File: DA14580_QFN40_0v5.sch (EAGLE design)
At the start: 29 parts, among them CON1 CON_TC2030-CTL-NL, IC1 1265-1137-1-ND, IC2 NC7SZ00M5XCT-ND, IC3 IC_LDO_XX1117_5, Q1 728-1076-1-ND, Q2 887-1833-1-ND, U1 DA14583-AT2, X1 SSW-114-02-S-S, X2 SSW-114-02-S-S

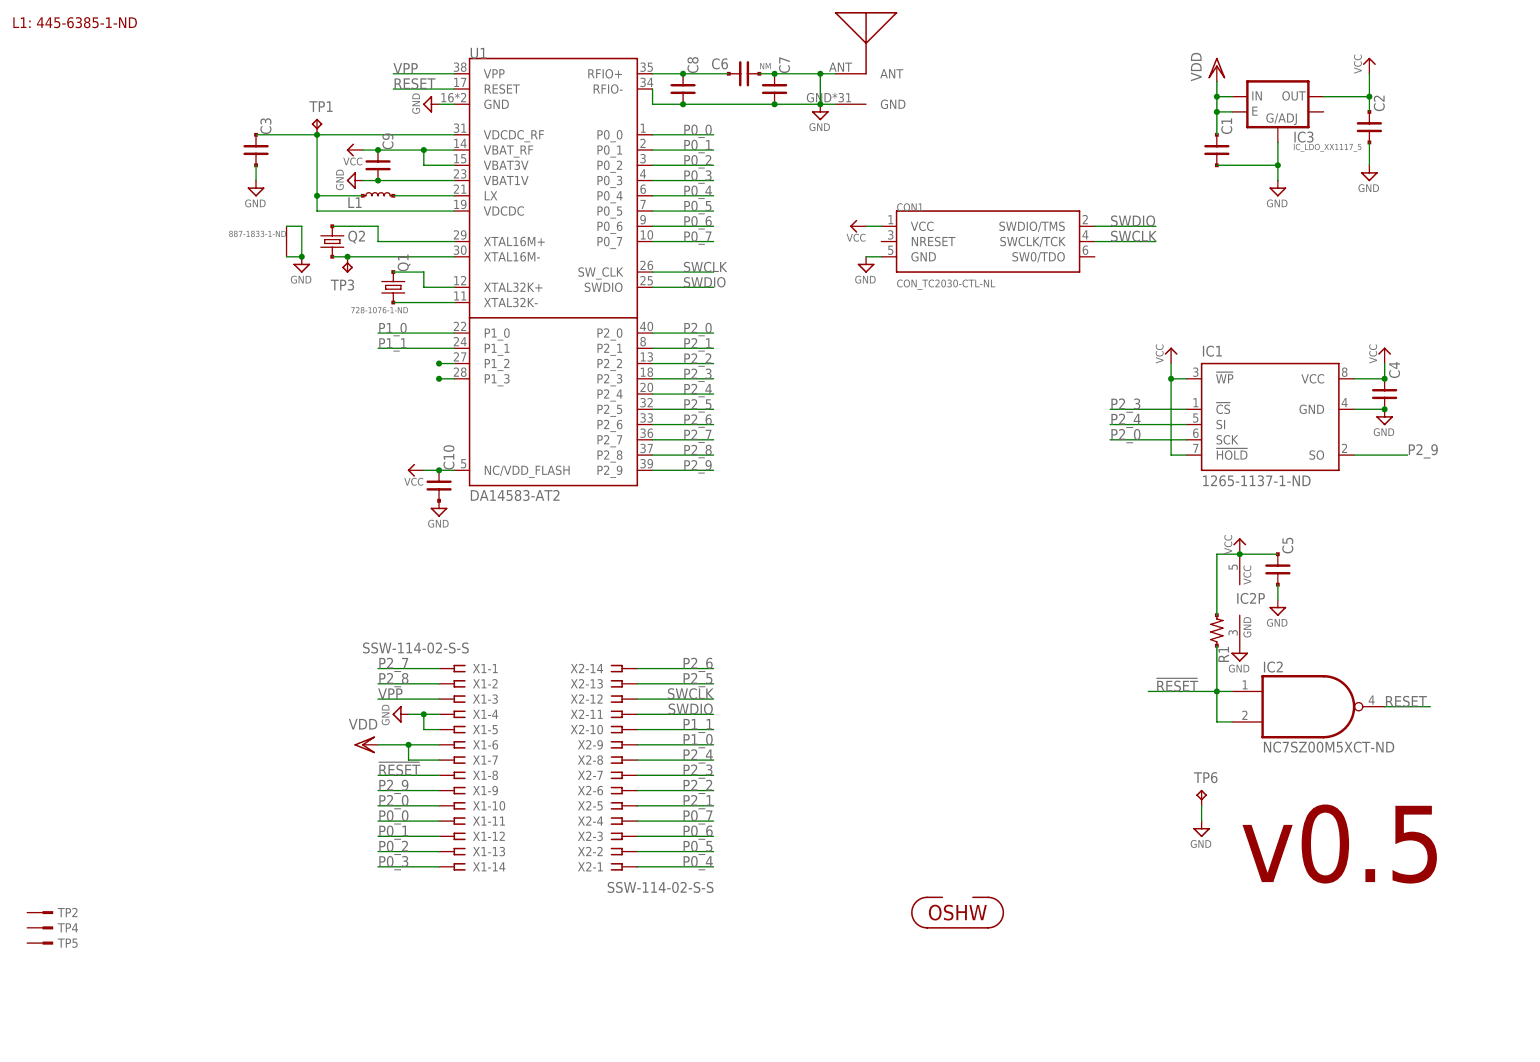
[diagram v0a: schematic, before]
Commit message: update eagle version: 7.5.0; library update
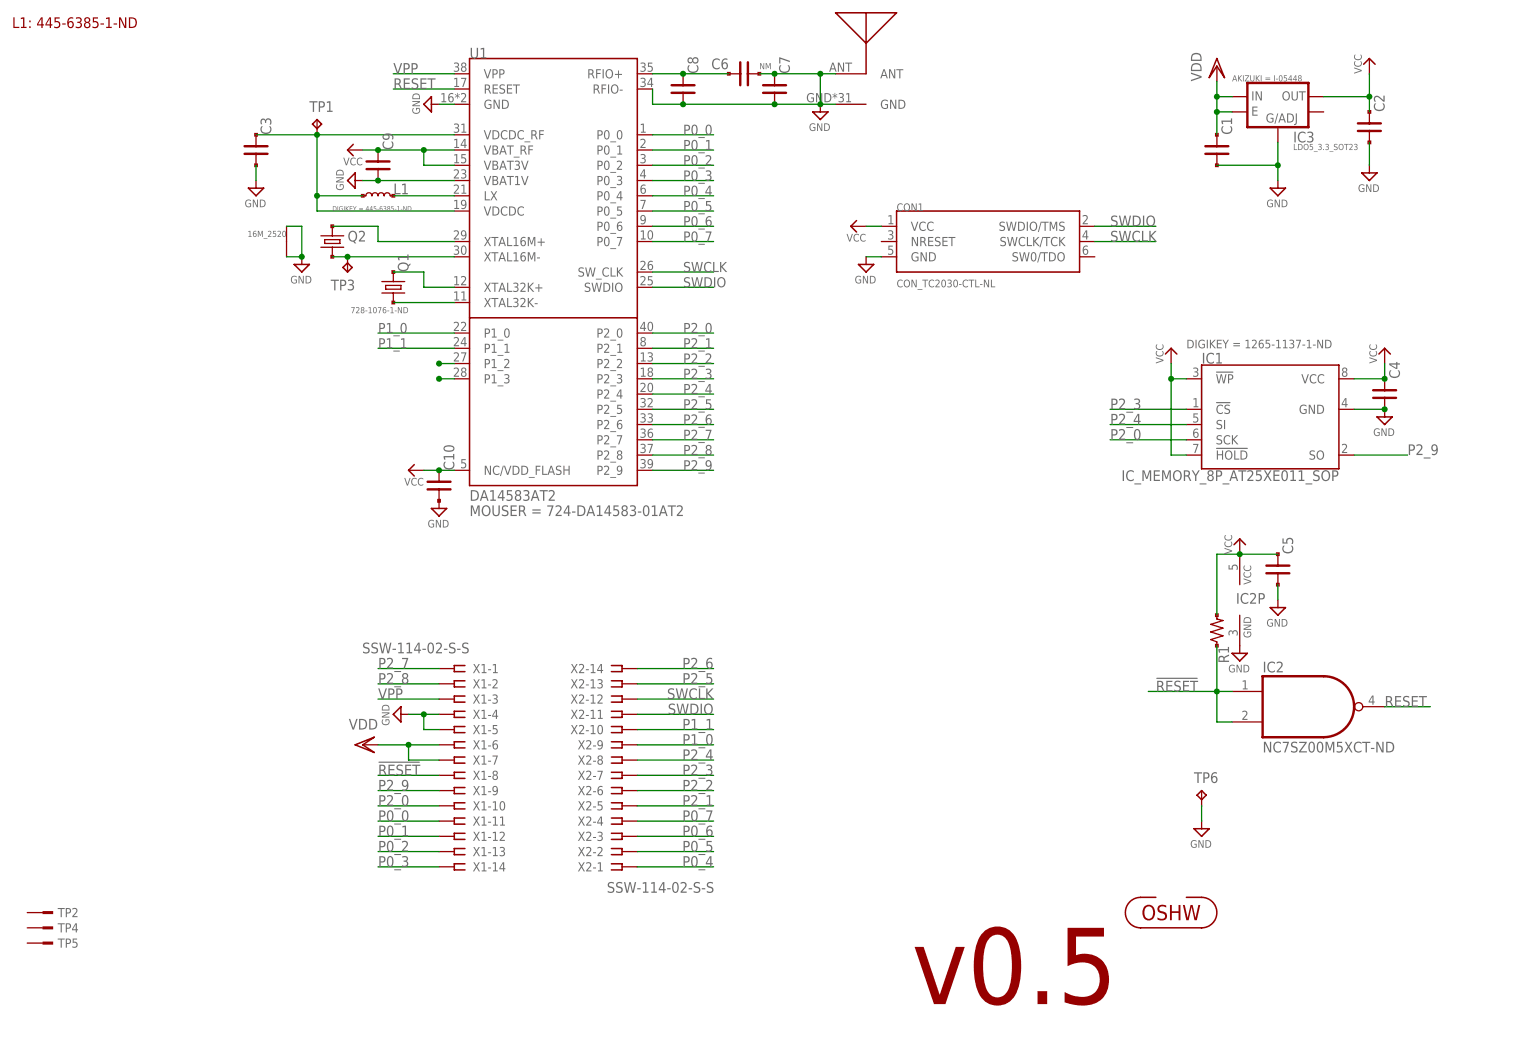
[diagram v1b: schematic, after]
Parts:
- IC1: value 1265-1137-1-ND -> IC_MEMORY_8P_AT25XE011_SOP
- IC3: value IC_LDO_XX1117_5 -> LDO5_3.3_SOT23; device mylib:IC_LDO_XX1117_5 -> mylib:LDO5_3.3_SOT23
- Q1: device mylib:CLOCK_CRYSTAL_FC-135 -> mylib:CRYSTAL2_32.768K_FC-135
- Q2: value 887-1833-1-ND -> 16M_2520; device mylib:CLOCK_CRYSTAL_4_2520 -> mylib:CRYSTAL4_16M_2520
- U1: value DA14583-AT2 -> DA14583AT2; device mylib:DA14583-AT2 -> mylib:DA14583AT2
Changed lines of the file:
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@@
 <?xml version="1.0" encoding="utf-8"?>
 <!DOCTYPE eagle SYSTEM "eagle.dtd">
-<eagle version="6.5.0">
+<eagle version="7.5.0">
 <drawing>
 <settings>
@@
 <layer number="98" name="Guide" color="6" fill="1" visible="yes" active="yes"/>
 <layer number="100" name="Muster" color="7" fill="1" visible="no" active="no"/>
-<layer number="101" name="Patch_Top" color="12" fill="4" visible="yes" active="yes"/>
+<layer number="101" name="Attributes" color="7" fill="1" visible="yes" active="yes"/>
 <layer number="102" name="Vscore" color="7" fill="1" visible="yes" active="yes"/>
 <layer number="103" name="tMap" color="7" fill="1" visible="yes" active="yes"/>
@@
 <layer number="111" name="LPC17xx" color="7" fill="1" visible="yes" active="yes"/>
 <layer number="112" name="tSilk" color="7" fill="1" visible="yes" active="yes"/>
-<layer number="113" name="FRNTTEKEN" color="7" fill="1" visible="no" active="yes"/>
-<layer number="114" name="FRNTMAAT1" color="7" fill="1" visible="no" active="yes"/>
-<layer number="115" name="FRNTMAAT2" color="7" fill="1" visible="no" active="yes"/>
+<layer number="113" name="FRNTTEKEN" color="7" fill="1" visible="yes" active="yes"/>
+<layer number="114" name="FRNTMAAT1" color="7" fill="1" visible="yes" active="yes"/>
+<layer number="115" name="FRNTMAAT2" color="7" fill="1" visible="yes" active="yes"/>
 <layer number="116" name="Patch_BOT" color="9" fill="4" visible="yes" active="yes"/>
-<layer number="117" name="BACKMAAT1" color="7" fill="1" visible="no" active="yes"/>
-<layer number="118" name="BACKMAAT2" color="7" fill="1" visible="no" active="yes"/>
-<layer number="119" name="KAP_TEKEN" color="7" fill="1" visible="no" active="yes"/>
-<layer number="120" name="KAP_MAAT1" color="7" fill="1" visible="no" active="yes"/>
+<layer number="117" name="BACKMAAT1" color="7" fill="1" visible="yes" active="yes"/>
+<layer number="118" name="BACKMAAT2" color="7" fill="1" visible="yes" active="yes"/>
+<layer number="119" name="KAP_TEKEN" color="7" fill="1" visible="yes" active="yes"/>
+<layer number="120" name="KAP_MAAT1" color="7" fill="1" visible="yes" active="yes"/>
 <layer number="121" name="_tsilk" color="7" fill="1" visible="yes" active="yes"/>
 <layer number="122" name="_bsilk" color="7" fill="1" visible="yes" active="yes"/>
@@
 <layer number="127" name="_tValues" color="7" fill="1" visible="yes" active="yes"/>
 <layer number="128" name="_bValues" color="7" fill="1" visible="yes" active="yes"/>
-<layer number="130" name="SMDSTROOK" color="7" fill="1" visible="no" active="yes"/>
+<layer number="130" name="SMDSTROOK" color="7" fill="1" visible="yes" active="yes"/>
 <layer number="131" name="tAdjust" color="7" fill="1" visible="no" active="yes"/>
 <layer number="132" name="bAdjust" color="7" fill="1" visible="no" active="yes"/>
 <layer number="144" name="Drill_legend" color="7" fill="1" visible="yes" active="yes"/>
-<layer number="145" name="DrillLegend_01-16" color="2" fill="9" visible="no" active="yes"/>
-<layer number="146" name="DrillLegend_01-20" color="3" fill="9" visible="no" active="yes"/>
 <layer number="151" name="HeatSink" color="7" fill="1" visible="yes" active="yes"/>
 <layer number="152" name="_bDocu" color="7" fill="1" visible="yes" active="yes"/>
@@
 <layer number="223" name="223bmp" color="24" fill="1" visible="no" active="no"/>
 <layer number="224" name="224bmp" color="25" fill="1" visible="no" active="no"/>
-<layer number="230" name="230bmp" color="7" fill="1" visible="no" active="yes"/>
+<layer number="230" name="230bmp" color="7" fill="1" visible="yes" active="yes"/>
 <layer number="248" name="Housing" color="7" fill="1" visible="yes" active="yes"/>
 <layer number="249" name="Edge" color="7" fill="1" visible="yes" active="yes"/>
@@
 <layer number="251" name="SMDround" color="4" fill="9" visible="no" active="yes"/>
 <layer number="254" name="cooling" color="7" fill="1" visible="yes" active="yes"/>
-<layer number="255" name="Accent" color="7" fill="1" visible="no" active="yes"/>
+<layer number="255" name="Accent" color="7" fill="1" visible="yes" active="yes"/>
 </layers>
 <schematic>
@@
 <parts>
 <part name="FRAME1" library="frames" deviceset="A4L-LOC" device="" value="A4L-LOC"/>
-<part name="U1" library="mylib" deviceset="DA1458*" device="-AT2" technology="3" value="DA14583-AT2"/>
+<part name="U1" library="mylib" deviceset="DA1458*" device="AT2" technology="3" value="DA14583AT2"/>
 <part name="SUPPLY1" library="mylib" deviceset="GND" device=""/>
 <part name="SUPPLY2" library="mylib" deviceset="GND" device=""/>
@@
 <part name="VDD1" library="supply1" deviceset="VDD" device=""/>
 <part name="P+1" library="mylib" deviceset="VCC" device=""/>
-<part name="Q1" library="mylib" deviceset="CLOCK_CRYSTAL" device="_FC-135" value="728-1076-1-ND"/>
+<part name="Q1" library="mylib" deviceset="CRYSTAL2_*" device="_FC-135" technology="32.768K" value="728-1076-1-ND"/>
 <part name="SUPPLY7" library="mylib" deviceset="GND" device=""/>
 <part name="SUPPLY8" library="mylib" deviceset="GND" device=""/>
@@
 <part name="L1" library="mylib" deviceset="INDUCTOR_" device="_1608" technology="2.2U" value=""/>
 <part name="R1" library="mylib" deviceset="R_US_*" device="_1005" technology="10K"/>
-<part name="IC1" library="mylib" deviceset="IC_MEMORY_8P_*" device="_SOP" technology="AT25XE011" value="1265-1137-1-ND"/>
+<part name="IC1" library="mylib" deviceset="IC_MEMORY_8P_*" device="_SOP" technology="AT25XE011" value="IC_MEMORY_8P_AT25XE011_SOP"/>
 <part name="P+3" library="mylib" deviceset="VCC" device=""/>
 <part name="C4" library="mylib" deviceset="C_SMD_*" device="_1005" technology="0.1U"/>
@@
 <part name="TP3" library="testpad_local" deviceset="TP" device="TP07R" value="TPTP07R"/>
 <part name="P+5" library="mylib" deviceset="VCC" device=""/>
-<part name="IC3" library="mylib" deviceset="IC_LDO_XX1117_5" device=""/>
+<part name="IC3" library="mylib" deviceset="LDO5_*" device="_SOT23" technology="3.3" value="LDO5_3.3_SOT23"/>
 <part name="IC2" library="74xx-little-us_local" deviceset="74*1G00" device="DBV" technology="LVC" value="NC7SZ00M5XCT-ND"/>
 <part name="TP6" library="testpad_local" deviceset="TP" device="PAD1-13"/>
@@
 <part name="U$2" library="mylib" deviceset="ICON_OSHW" device=""/>
 <part name="P+6" library="mylib" deviceset="VCC" device=""/>
-<part name="Q2" library="mylib" deviceset="CLOCK_CRYSTAL_4" device="_2520" value="887-1833-1-ND"/>
+<part name="Q2" library="mylib" deviceset="CRYSTAL4_*" device="_2520" technology="16M" value="16M_2520"/>
 <part name="P+7" library="mylib" deviceset="VCC" device=""/>
 <part name="TP2" library="mylib" deviceset="TESTPAD" device="_F"/>
@@
 <sheet>
 <plain>
-<text x="217.17" y="25.4" size="12.7" layer="94">v0.5</text>
+<text x="162.56" y="5.08" size="12.7" layer="94">v0.5</text>
 <text x="12.7" y="167.64" size="1.778" layer="94">L1: 445-6385-1-ND</text>
 </plain>
 <instances>
 <instance part="FRAME1" gate="G$1" x="0" y="0"/>
-<instance part="U1" gate="G$1" x="104.14" y="142.24"/>
+<instance part="U1" gate="G$1" x="104.14" y="142.24">
+<attribute name="MOUSER" x="88.9" y="86.36" size="1.778" layer="96" display="both"/>
+</instance>
 <instance part="SUPPLY1" gate="GND" x="81.28" y="154.94" rot="R270"/>
 <instance part="SUPPLY2" gate="GND" x="147.32" y="152.4"/>
@@
 </instance>
 <instance part="L1" gate="G$1" x="73.66" y="139.7" smashed="yes">
-<attribute name="NAME" x="71.12" y="139.446" size="1.778" layer="95" rot="R180"/>
-<attribute name="VALUE" x="71.12" y="137.668" size="1.016" layer="96"/>
+<attribute name="DIGIKEY" x="66.04" y="137.16" size="0.8128" layer="96" display="both"/>
+<attribute name="NAME" x="76.2" y="139.954" size="1.778" layer="95"/>
+<attribute name="VALUE" x="76.2" y="137.668" size="1.016" layer="96"/>
 </instance>
 <instance part="R1" gate="G$1" x="213.36" y="67.31" rot="R90"/>
-<instance part="IC1" gate="G$1" x="223.52" y="101.6"/>
+<instance part="IC1" gate="G$1" x="223.52" y="101.6">
+<attribute name="DIGIKEY" x="208.28" y="114.3" size="1.4224" layer="96" display="both"/>
+</instance>
 <instance part="P+3" gate="VCC" x="205.74" y="114.3"/>
 <instance part="C4" gate="G$1" x="241.3" y="106.68"/>
@@
 </instance>
 <instance part="P+5" gate="VCC" x="78.74" y="93.98" rot="R90"/>
-<instance part="IC3" gate="G$1" x="223.52" y="158.75"/>
+<instance part="IC3" gate="G$1" x="223.52" y="158.75">
+<attribute name="AKIZUKI" x="215.9" y="158.75" size="1.016" layer="96" display="both"/>
+</instance>
 <instance part="IC2" gate="A" x="228.6" y="54.61"/>
 <instance part="IC2" gate="P" x="217.17" y="72.39"/>
@@
 <instance part="CON1" gate="G$1" x="175.26" y="132.08"/>
 <instance part="SUPPLY5" gate="GND" x="154.94" y="127"/>
-<instance part="U$2" gate="G$1" x="170.18" y="20.32"/>
+<instance part="U$2" gate="G$1" x="205.74" y="20.32"/>
 <instance part="P+6" gate="VCC" x="152.4" y="134.62" rot="R90"/>
 <instance part="Q2" gate="G$1" x="66.04" y="132.08" smashed="yes" rot="R270">
